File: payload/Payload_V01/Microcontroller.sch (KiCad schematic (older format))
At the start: 1 part, among them U4 STM32F407VETx

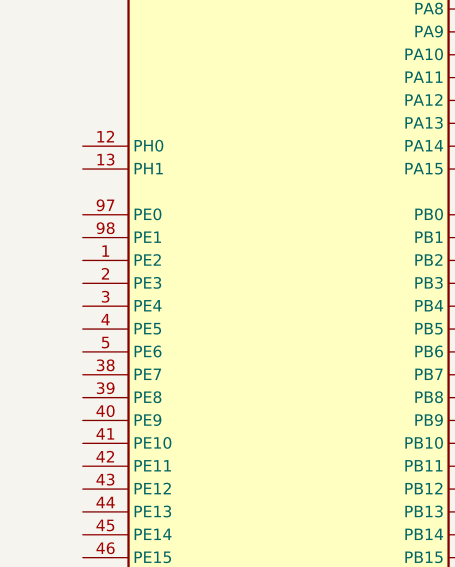
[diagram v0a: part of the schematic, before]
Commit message: tested labels to get microcontroller working
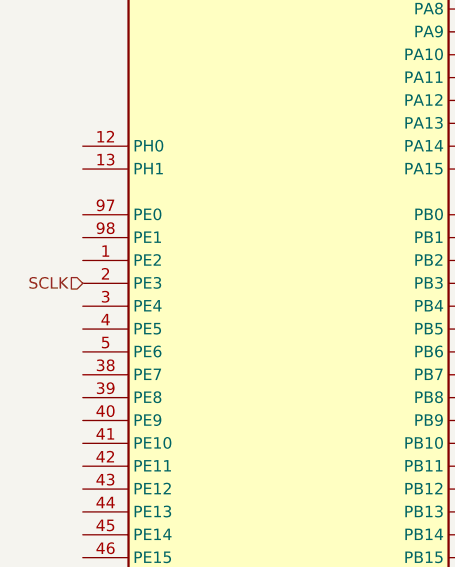
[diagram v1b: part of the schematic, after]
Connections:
- net SCLK: now reaches U4.2 (PE3)
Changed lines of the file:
@@
 	1    0    0    -1
 $EndComp
+Text HLabel 4450 3450 0    50   Input ~ 0
+SCLK
 $EndSCHEMATC

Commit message: small change
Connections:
- net SCLK: no longer names the net of U4.2 (PE3)
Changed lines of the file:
@@
 	1    0    0    -1
 $EndComp
-Text HLabel 4450 3450 0    50   Input ~ 0
-SCLK
 $EndSCHEMATC
